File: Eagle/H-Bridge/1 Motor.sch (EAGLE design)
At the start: 10 parts, among them K1 CQ1-12V, K2 CQ1-12V, T3 TIP122

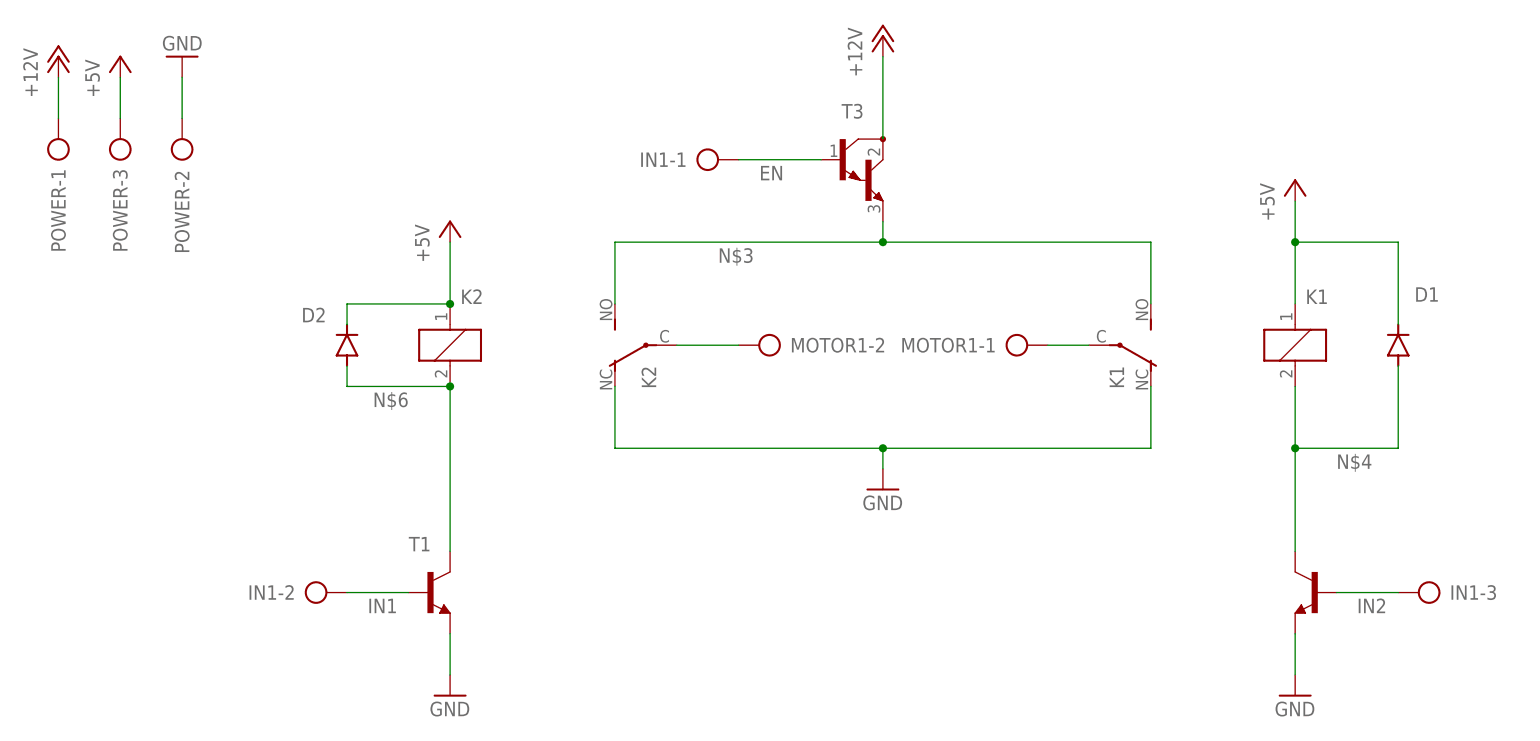
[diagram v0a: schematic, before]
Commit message: re-arrange items and use the right package of the relay.
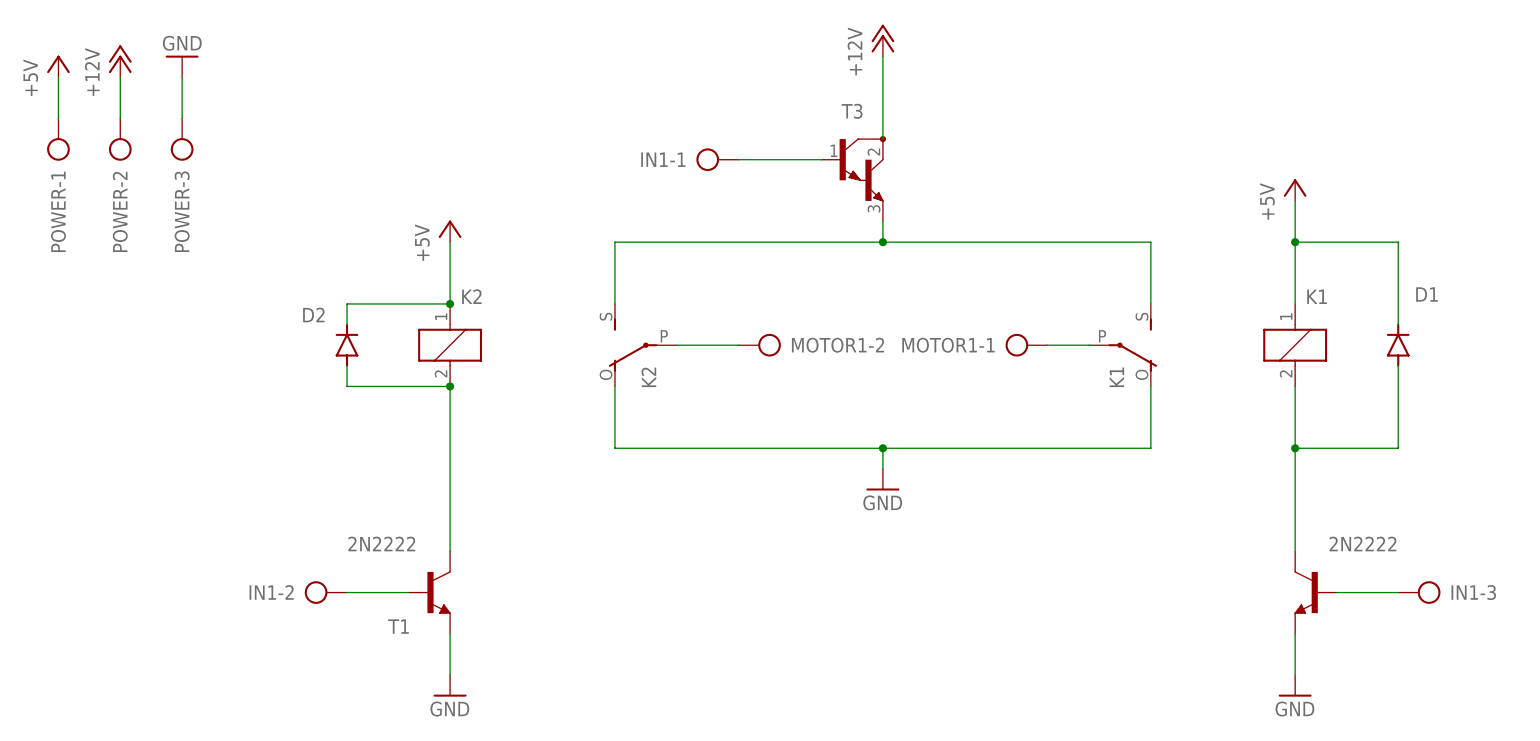
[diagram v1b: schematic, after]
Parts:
- K1, K2: value CQ1-12V -> ZF112; device relay:CQ1-12V -> relay:ZF112
- T1, T2: value (none) -> 2N2222
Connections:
- net N$3 renamed NO
- net +12V: now also POWER-2.KL; no longer POWER-1.KL
- net +5V: now also POWER-1.KL; no longer POWER-3.KL
- net GND: now also POWER-3.KL; no longer POWER-2.KL
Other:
- moved on the sheet: POWER-2, POWER-3
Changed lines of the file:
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@@
 </classes>
 <parts>
-<part name="K1" library="relay" deviceset="CQ1-12V" device="" package3d_urn="urn:adsk.eagle:package:27138158/2"/>
-<part name="K2" library="relay" deviceset="CQ1-12V" device="" package3d_urn="urn:adsk.eagle:package:27138158/2"/>
+<part name="K1" library="relay" library_urn="urn:adsk.eagle:library:28981693" deviceset="ZF112" device="" package3d_urn="urn:adsk.eagle:package:28981678/3"/>
+<part name="K2" library="relay" library_urn="urn:adsk.eagle:library:28981693" deviceset="ZF112" device="" package3d_urn="urn:adsk.eagle:package:28981678/3"/>
 <part name="MOTOR1" library="con-ptr500" deviceset="AK300/2" device="" package3d_urn="urn:adsk.eagle:package:27135568/2"/>
 <part name="POWER" library="con-ptr500" deviceset="AK300/3" device="" package3d_urn="urn:adsk.eagle:package:27135583/2"/>
 <part name="D1" library="diode" deviceset="1N4004" device="" package3d_urn="urn:adsk.eagle:package:27138186/3"/>
 <part name="D2" library="diode" deviceset="1N4004" device="" package3d_urn="urn:adsk.eagle:package:27138186/3"/>
-<part name="T1" library="transistor-neu-to92" library_urn="urn:adsk.eagle:library:397" deviceset="*-NPN-" device="TO92-EBC" package3d_urn="urn:adsk.eagle:package:28763/2" technology="2N2222"/>
-<part name="T2" library="transistor-neu-to92" library_urn="urn:adsk.eagle:library:397" deviceset="*-NPN-" device="TO92-EBC" package3d_urn="urn:adsk.eagle:package:28763/2" technology="2N2222"/>
+<part name="T1" library="transistor-neu-to92" library_urn="urn:adsk.eagle:library:397" deviceset="*-NPN-" device="TO92-EBC" package3d_urn="urn:adsk.eagle:package:28763/2" technology="2N2222" value="2N2222"/>
+<part name="T2" library="transistor-neu-to92" library_urn="urn:adsk.eagle:library:397" deviceset="*-NPN-" device="TO92-EBC" package3d_urn="urn:adsk.eagle:package:28763/2" technology="2N2222" value="2N2222"/>
 <part name="T3" library="transistor" deviceset="TIP122" device="" package3d_urn="urn:adsk.eagle:package:27138341/2"/>
 <part name="IN1" library="con-ptr500" deviceset="AK300/3" device="" package3d_urn="urn:adsk.eagle:package:27135583/2"/>
 <part name="P+1" library="supply1" library_urn="urn:adsk.eagle:library:371" deviceset="+12V" device=""/>
-<part name="P+2" library="supply1" library_urn="urn:adsk.eagle:library:371" deviceset="+5V" device=""/>
-<part name="GND1" library="supply1" library_urn="urn:adsk.eagle:library:371" deviceset="GND" device=""/>
-<part name="P+3" library="supply1" library_urn="urn:adsk.eagle:library:371" deviceset="+12V" device=""/>
 <part name="P+4" library="supply1" library_urn="urn:adsk.eagle:library:371" deviceset="+5V" device=""/>
 <part name="P+5" library="supply1" library_urn="urn:adsk.eagle:library:371" deviceset="+5V" device=""/>
@@
 <part name="GND3" library="supply1" library_urn="urn:adsk.eagle:library:371" deviceset="GND" device=""/>
 <part name="GND4" library="supply1" library_urn="urn:adsk.eagle:library:371" deviceset="GND" device=""/>
+<part name="GND1" library="supply1" library_urn="urn:adsk.eagle:library:371" deviceset="GND" device=""/>
+<part name="P+2" library="supply1" library_urn="urn:adsk.eagle:library:371" deviceset="+5V" device=""/>
+<part name="P+3" library="supply1" library_urn="urn:adsk.eagle:library:371" deviceset="+12V" device=""/>
 </parts>
 <sheets>
@@
 </instance>
 <instance part="POWER" gate="-1" x="-25.4" y="81.28" smashed="yes" rot="R90">
-<attribute name="NAME" x="-24.511" y="69.85" size="1.778" layer="95" rot="R90"/>
-</instance>
-<instance part="POWER" gate="-2" x="-10.16" y="81.28" smashed="yes" rot="R90">
+<attribute name="NAME" x="-26.289" y="80.01" size="1.778" layer="95" rot="R270"/>
+</instance>
+<instance part="POWER" gate="-2" x="-17.78" y="81.28" smashed="yes" rot="R90">
+<attribute name="NAME" x="-18.669" y="80.01" size="1.778" layer="95" rot="R270"/>
+</instance>
+<instance part="POWER" gate="-3" x="-10.16" y="81.28" smashed="yes" rot="R90">
 <attribute name="NAME" x="-11.049" y="80.01" size="1.778" layer="95" rot="R270"/>
-</instance>
-<instance part="POWER" gate="-3" x="-17.78" y="81.28" smashed="yes" rot="R90">
-<attribute name="NAME" x="-16.891" y="69.85" size="1.778" layer="95" rot="R90"/>
-<attribute name="VALUE" x="-14.097" y="77.47" size="1.778" layer="96" rot="R90"/>
+<attribute name="VALUE" x="-6.477" y="77.47" size="1.778" layer="96" rot="R90"/>
 </instance>
 <instance part="D1" gate="1" x="139.7" y="58.42" smashed="yes" rot="R90">
@@
 </instance>
 <instance part="T1" gate="G$1" x="20.32" y="27.94" smashed="yes">
-<attribute name="NAME" x="17.78" y="33.02" size="1.778" layer="95"/>
+<attribute name="NAME" x="15.24" y="22.86" size="1.778" layer="95"/>
 <attribute name="VALUE" x="10.16" y="33.02" size="1.778" layer="96"/>
 </instance>
@@
 <attribute name="VALUE" x="73.66" y="91.44" size="1.778" layer="96" rot="R90"/>
 </instance>
-<instance part="P+2" gate="1" x="-17.78" y="93.98" smashed="yes">
-<attribute name="VALUE" x="-20.32" y="88.9" size="1.778" layer="96" rot="R90"/>
+<instance part="P+4" gate="1" x="22.86" y="73.66" smashed="yes">
+<attribute name="VALUE" x="20.32" y="68.58" size="1.778" layer="96" rot="R90"/>
+</instance>
+<instance part="P+5" gate="1" x="127" y="78.74" smashed="yes">
+<attribute name="VALUE" x="124.46" y="73.66" size="1.778" layer="96" rot="R90"/>
+</instance>
+<instance part="GND2" gate="1" x="22.86" y="15.24" smashed="yes">
+<attribute name="VALUE" x="20.32" y="12.7" size="1.778" layer="96"/>
+</instance>
+<instance part="GND3" gate="1" x="127" y="15.24" smashed="yes">
+<attribute name="VALUE" x="124.46" y="12.7" size="1.778" layer="96"/>
+</instance>
+<instance part="GND4" gate="1" x="76.2" y="40.64" smashed="yes">
+<attribute name="VALUE" x="73.66" y="38.1" size="1.778" layer="96"/>
 </instance>
 <instance part="GND1" gate="1" x="-10.16" y="93.98" smashed="yes" rot="R180">
 <attribute name="VALUE" x="-7.62" y="96.52" size="1.778" layer="96" rot="R180"/>
 </instance>
-<instance part="P+3" gate="1" x="-25.4" y="93.98" smashed="yes">
+<instance part="P+2" gate="1" x="-25.4" y="93.98" smashed="yes">
 <attribute name="VALUE" x="-27.94" y="88.9" size="1.778" layer="96" rot="R90"/>
 </instance>
-<instance part="P+4" gate="1" x="22.86" y="73.66" smashed="yes">
-<attribute name="VALUE" x="20.32" y="68.58" size="1.778" layer="96" rot="R90"/>
-</instance>
-<instance part="P+5" gate="1" x="127" y="78.74" smashed="yes">
-<attribute name="VALUE" x="124.46" y="73.66" size="1.778" layer="96" rot="R90"/>
-</instance>
-<instance part="GND2" gate="1" x="22.86" y="15.24" smashed="yes">
-<attribute name="VALUE" x="20.32" y="12.7" size="1.778" layer="96"/>
-</instance>
-<instance part="GND3" gate="1" x="127" y="15.24" smashed="yes">
-<attribute name="VALUE" x="124.46" y="12.7" size="1.778" layer="96"/>
-</instance>
-<instance part="GND4" gate="1" x="76.2" y="40.64" smashed="yes">
-<attribute name="VALUE" x="73.66" y="38.1" size="1.778" layer="96"/>
+<instance part="P+3" gate="1" x="-17.78" y="93.98" smashed="yes">
+<attribute name="VALUE" x="-20.32" y="88.9" size="1.778" layer="96" rot="R90"/>
 </instance>
 </instances>
@@
 </segment>
 <segment>
+<pinref part="POWER" gate="-2" pin="KL"/>
+<wire x1="-17.78" y1="86.36" x2="-17.78" y2="91.44" width="0.1524" layer="91"/>
 <pinref part="P+3" gate="1" pin="+12V"/>
-<pinref part="POWER" gate="-1" pin="KL"/>
-<wire x1="-25.4" y1="86.36" x2="-25.4" y2="91.44" width="0.1524" layer="91"/>
 </segment>
 </net>
@@
 <wire x1="10.16" y1="53.34" x2="22.86" y2="53.34" width="0.1524" layer="91"/>
 <junction x="22.86" y="53.34"/>
-<label x="17.78" y="50.8" size="1.778" layer="95" rot="MR0"/>
 </segment>
 </net>
@@
 <wire x1="127" y1="33.02" x2="127" y2="45.72" width="0.1524" layer="91"/>
 <junction x="127" y="45.72"/>
-<label x="132.08" y="43.18" size="1.778" layer="95"/>
-</segment>
-</net>
-<net name="N$3" class="0">
+</segment>
+</net>
+<net name="NO" class="0">
 <segment>
 <pinref part="T3" gate="G$1" pin="E"/>
@@
 <wire x1="109.22" y1="71.12" x2="76.2" y2="71.12" width="0.1524" layer="91"/>
 <junction x="76.2" y="71.12"/>
-<label x="55.88" y="68.58" size="1.778" layer="95"/>
 </segment>
 </net>
@@
 </segment>
 <segment>
+<pinref part="POWER" gate="-1" pin="KL"/>
+<wire x1="-25.4" y1="86.36" x2="-25.4" y2="91.44" width="0.1524" layer="91"/>
 <pinref part="P+2" gate="1" pin="+5V"/>
-<pinref part="POWER" gate="-3" pin="KL"/>
-<wire x1="-17.78" y1="86.36" x2="-17.78" y2="91.44" width="0.1524" layer="91"/>
 </segment>
 </net>
@@
 </segment>
 <segment>
+<pinref part="POWER" gate="-3" pin="KL"/>
+<wire x1="-10.16" y1="86.36" x2="-10.16" y2="91.44" width="0.1524" layer="91"/>
 <pinref part="GND1" gate="1" pin="GND"/>
-<pinref part="POWER" gate="-2" pin="KL"/>
-<wire x1="-10.16" y1="86.36" x2="-10.16" y2="91.44" width="0.1524" layer="91"/>
 </segment>
 </net>
@@
 <pinref part="IN1" gate="-1" pin="KL"/>
 <wire x1="58.42" y1="81.28" x2="68.58" y2="81.28" width="0.1524" layer="91"/>
-<label x="60.96" y="78.74" size="1.778" layer="95"/>
 </segment>
 </net>
@@
 <wire x1="10.16" y1="27.94" x2="17.78" y2="27.94" width="0.1524" layer="91"/>
 <pinref part="IN1" gate="-2" pin="KL"/>
-<label x="12.7" y="25.4" size="1.778" layer="95"/>
 </segment>
 </net>
@@
 <pinref part="IN1" gate="-3" pin="KL"/>
 <wire x1="139.7" y1="27.94" x2="132.08" y2="27.94" width="0.1524" layer="91"/>
-<label x="134.62" y="25.4" size="1.778" layer="95"/>
-</segment>
-</net>
+</segment>
+</net>
